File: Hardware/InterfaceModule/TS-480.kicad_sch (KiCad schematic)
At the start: 5 parts, among them J3 TS-480 MIC, J4 TS-480 DATA, J5 TS-480 REMOTE, J6 TS-480 COM, J7 TS-480 EXT.SP

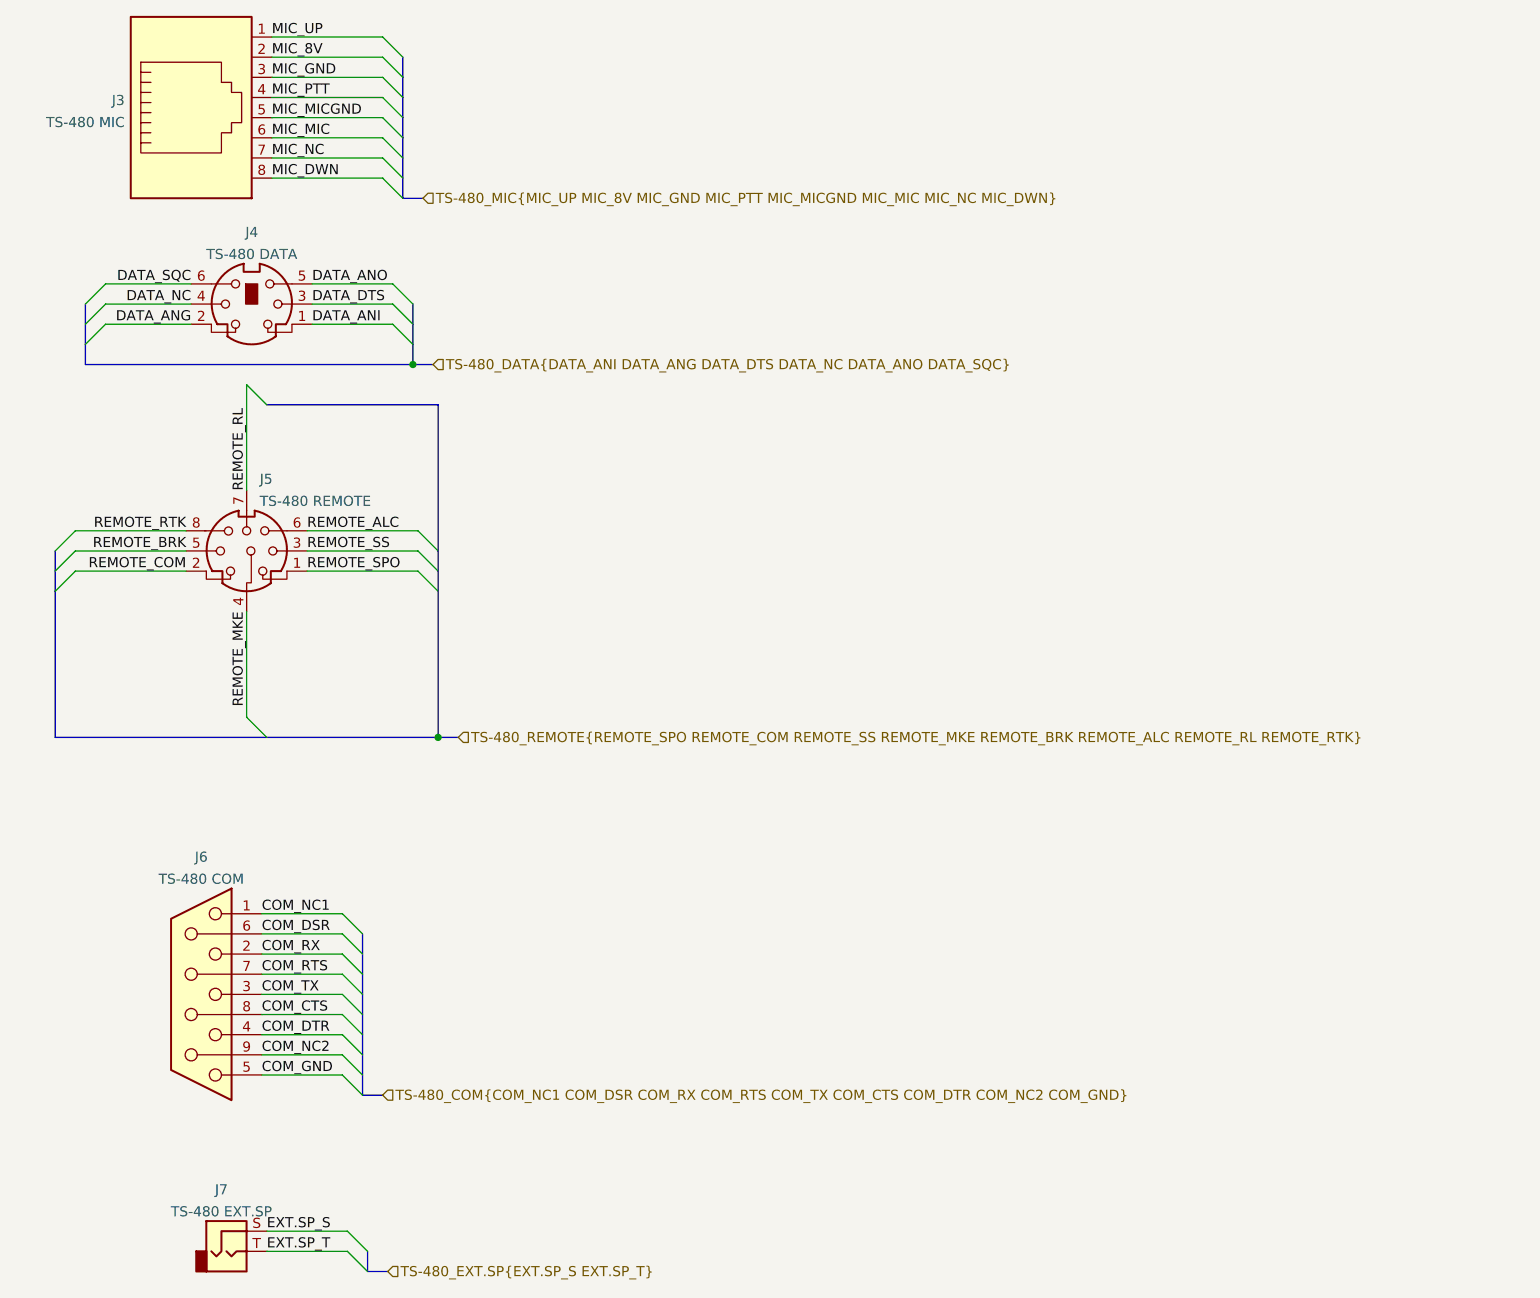
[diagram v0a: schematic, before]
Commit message: Connections for data ports, gps, improved mic connections
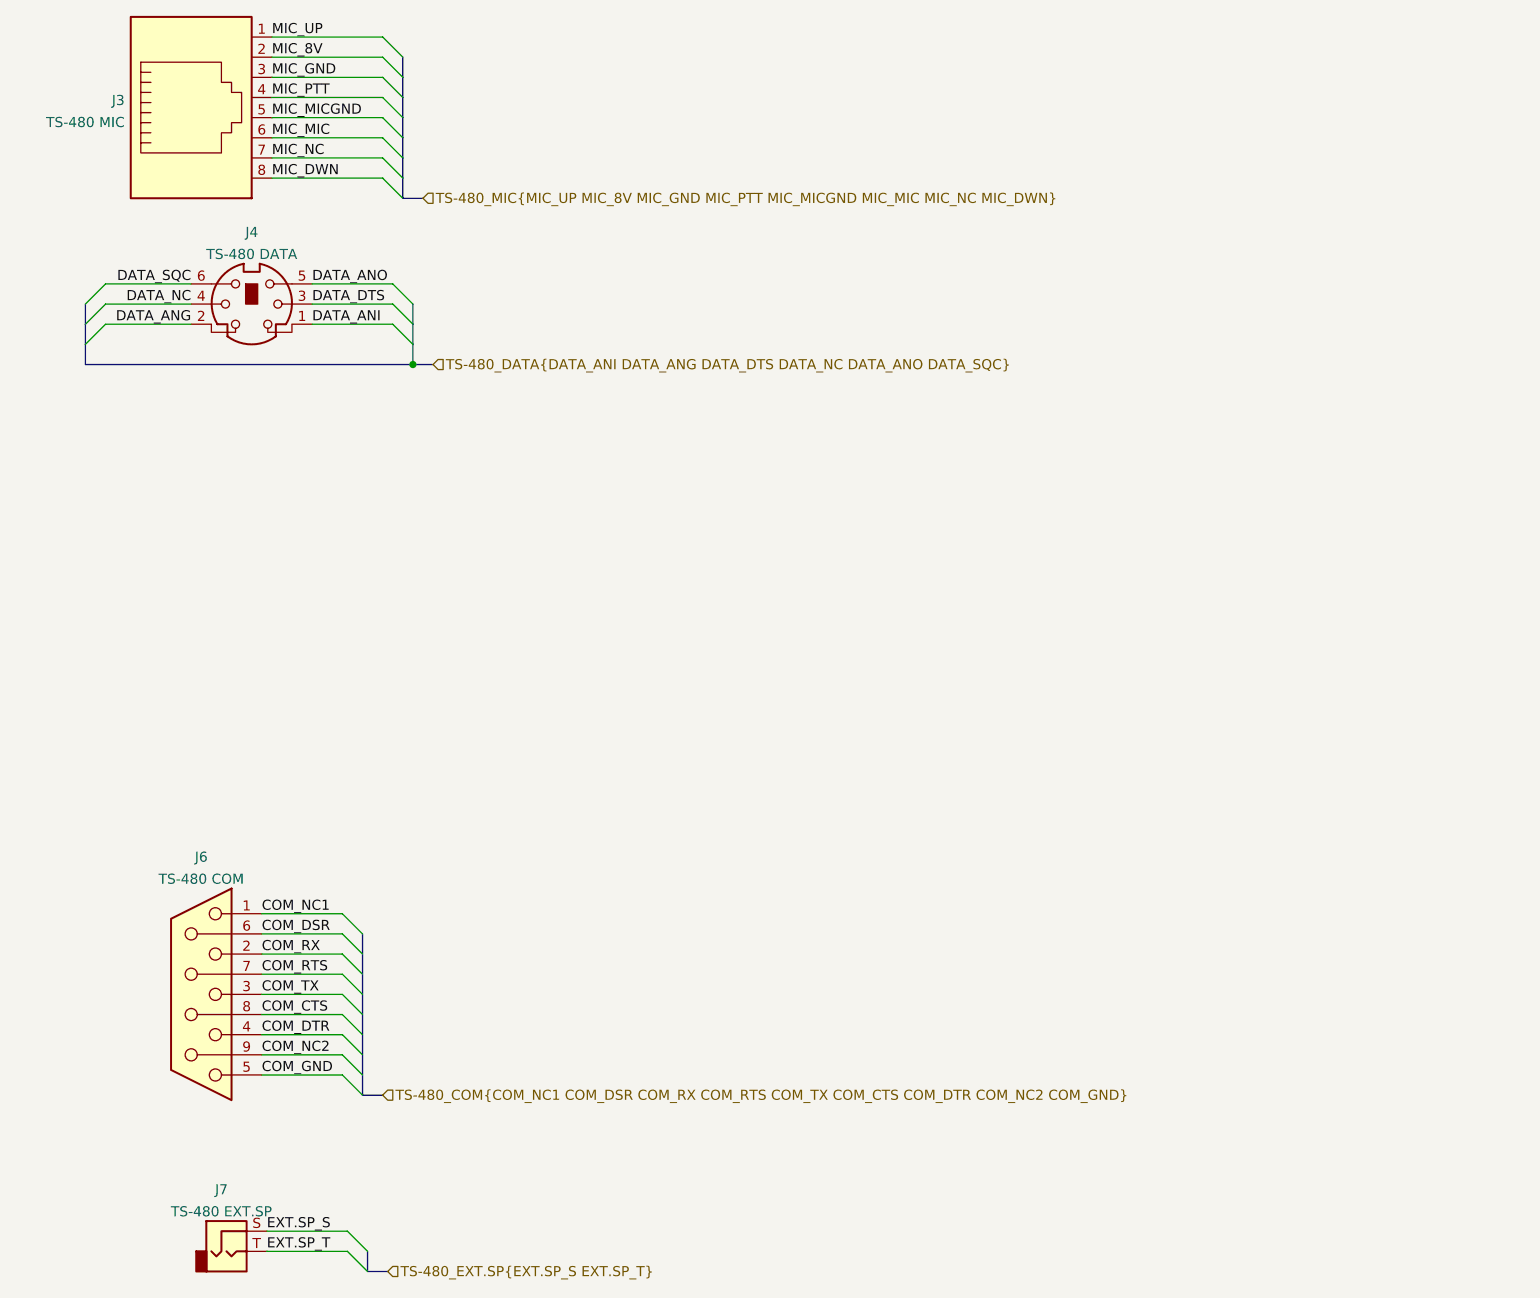
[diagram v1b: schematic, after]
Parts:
- removed J5: TS-480 REMOTE, symbol Connector:Mini-DIN-8
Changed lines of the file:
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@@
 (kicad_sch (version 20211123) (generator eeschema)
   (paper "A4")
-  (junction (at 64.77 107.95) (diameter 0) (color 0 0 0 0)
-  )
   (junction (at 61.595 60.96) (diameter 0) (color 0 0 0 0)
   )
@@
     (stroke (width 0) (type default) (color 0 0 0 0))
   )
-  (bus_entry (at 40.64 63.5) (size 2.54 2.54)
-    (stroke (width 0) (type default) (color 0 0 0 0))
-  )
-  (bus_entry (at 40.64 105.41) (size 2.54 2.54)
-    (stroke (width 0) (type default) (color 0 0 0 0))
-  )
-  (bus_entry (at 19.05 84.455) (size -2.54 2.54)
-    (stroke (width 0) (type default) (color 0 0 0 0))
-  )
-  (bus_entry (at 19.05 81.915) (size -2.54 2.54)
-    (stroke (width 0) (type default) (color 0 0 0 0))
-  )
-  (bus_entry (at 19.05 86.995) (size -2.54 2.54)
-    (stroke (width 0) (type default) (color 0 0 0 0))
-  )
-  (bus_entry (at 62.23 81.915) (size 2.54 2.54)
-    (stroke (width 0) (type default) (color 0 0 0 0))
-  )
-  (bus_entry (at 62.23 84.455) (size 2.54 2.54)
-    (stroke (width 0) (type default) (color 0 0 0 0))
-  )
-  (bus_entry (at 62.23 86.995) (size 2.54 2.54)
-    (stroke (width 0) (type default) (color 0 0 0 0))
-  )
   (bus (pts (xy 20.32 53.34) (xy 20.32 55.88))
     (stroke (width 0) (type default) (color 0 0 0 0))
   )
-  (bus (pts (xy 43.18 66.04) (xy 64.77 66.04))
-    (stroke (width 0) (type default) (color 0 0 0 0))
-  )
   (wire (pts (xy 22.86 50.8) (xy 33.655 50.8))
     (stroke (width 0) (type default) (color 0 0 0 0))
   )
-  (bus (pts (xy 64.77 84.455) (xy 64.77 66.04))
-    (stroke (width 0) (type default) (color 0 0 0 0))
-  )
   (wire (pts (xy 43.815 27.305) (xy 57.785 27.305))
     (stroke (width 0) (type default) (color 0 0 0 0))
@@
     (stroke (width 0) (type default) (color 0 0 0 0))
   )
-  (bus (pts (xy 64.77 107.95) (xy 64.77 89.535))
-    (stroke (width 0) (type default) (color 0 0 0 0))
-  )
   (wire (pts (xy 42.545 140.335) (xy 52.705 140.335))
     (stroke (width 0) (type default) (color 0 0 0 0))
@@
     (stroke (width 0) (type default) (color 0 0 0 0))
   )
-  (wire (pts (xy 40.64 92.075) (xy 40.64 105.41))
-    (stroke (width 0) (type default) (color 0 0 0 0))
-  )
-  (bus (pts (xy 16.51 84.455) (xy 16.51 86.995))
-    (stroke (width 0) (type default) (color 0 0 0 0))
-  )
-  (bus (pts (xy 16.51 107.95) (xy 43.18 107.95))
-    (stroke (width 0) (type default) (color 0 0 0 0))
-  )
   (wire (pts (xy 42.545 137.795) (xy 52.705 137.795))
     (stroke (width 0) (type default) (color 0 0 0 0))
   )
-  (wire (pts (xy 19.05 86.995) (xy 33.02 86.995))
-    (stroke (width 0) (type default) (color 0 0 0 0))
-  )
-  (bus (pts (xy 16.51 86.995) (xy 16.51 89.535))
-    (stroke (width 0) (type default) (color 0 0 0 0))
-  )
   (wire (pts (xy 48.895 55.88) (xy 59.055 55.88))
     (stroke (width 0) (type default) (color 0 0 0 0))
@@
     (stroke (width 0) (type default) (color 0 0 0 0))
   )
-  (wire (pts (xy 19.05 84.455) (xy 33.02 84.455))
-    (stroke (width 0) (type default) (color 0 0 0 0))
-  )
   (bus (pts (xy 60.325 24.765) (xy 60.325 27.305))
     (stroke (width 0) (type default) (color 0 0 0 0))
   )
-  (wire (pts (xy 48.26 81.915) (xy 62.23 81.915))
-    (stroke (width 0) (type default) (color 0 0 0 0))
-  )
   (bus (pts (xy 61.595 55.88) (xy 61.595 58.42))
     (stroke (width 0) (type default) (color 0 0 0 0))
   )
-  (bus (pts (xy 43.18 107.95) (xy 64.77 107.95))
-    (stroke (width 0) (type default) (color 0 0 0 0))
-  )
   (bus (pts (xy 60.325 34.925) (xy 60.325 37.465))
     (stroke (width 0) (type default) (color 0 0 0 0))
@@
     (stroke (width 0) (type default) (color 0 0 0 0))
   )
-  (wire (pts (xy 48.26 86.995) (xy 62.23 86.995))
-    (stroke (width 0) (type default) (color 0 0 0 0))
-  )
   (wire (pts (xy 42.545 147.955) (xy 52.705 147.955))
     (stroke (width 0) (type default) (color 0 0 0 0))
   )
-  (bus (pts (xy 16.51 89.535) (xy 16.51 107.95))
-    (stroke (width 0) (type default) (color 0 0 0 0))
-  )
   (bus (pts (xy 55.245 140.335) (xy 55.245 142.875))
     (stroke (width 0) (type default) (color 0 0 0 0))
@@
     (stroke (width 0) (type default) (color 0 0 0 0))
   )
-  (wire (pts (xy 40.64 63.5) (xy 40.64 76.835))
-    (stroke (width 0) (type default) (color 0 0 0 0))
-  )
   (bus (pts (xy 60.325 22.225) (xy 60.325 24.765))
     (stroke (width 0) (type default) (color 0 0 0 0))
@@
     (stroke (width 0) (type default) (color 0 0 0 0))
   )
-  (wire (pts (xy 19.05 81.915) (xy 33.02 81.915))
-    (stroke (width 0) (type default) (color 0 0 0 0))
-  )
-  (bus (pts (xy 64.77 86.995) (xy 64.77 84.455))
-    (stroke (width 0) (type default) (color 0 0 0 0))
-  )
   (wire (pts (xy 42.545 142.875) (xy 52.705 142.875))
     (stroke (width 0) (type default) (color 0 0 0 0))
   )
-  (bus (pts (xy 64.77 89.535) (xy 64.77 86.995))
-    (stroke (width 0) (type default) (color 0 0 0 0))
-  )
   (bus (pts (xy 55.245 137.795) (xy 55.245 140.335))
     (stroke (width 0) (type default) (color 0 0 0 0))
   )
-  (bus (pts (xy 64.77 107.95) (xy 67.31 107.95))
-    (stroke (width 0) (type default) (color 0 0 0 0))
-  )
   (wire (pts (xy 22.86 55.88) (xy 33.655 55.88))
     (stroke (width 0) (type default) (color 0 0 0 0))
@@
     (stroke (width 0) (type default) (color 0 0 0 0))
   )
-  (wire (pts (xy 48.26 84.455) (xy 62.23 84.455))
-    (stroke (width 0) (type default) (color 0 0 0 0))
-  )
   (bus (pts (xy 20.32 55.88) (xy 20.32 58.42))
     (stroke (width 0) (type default) (color 0 0 0 0))
@@
     (effects (font (size 1.27 1.27)) (justify left bottom))
   )
-  (label "REMOTE_RTK" (at 33.02 81.915 180)
-    (effects (font (size 1.27 1.27)) (justify right bottom))
-  )
-  (label "REMOTE_ALC" (at 48.26 81.915 0)
-    (effects (font (size 1.27 1.27)) (justify left bottom))
-  )
   (label "MIC_NC" (at 43.815 34.925 0)
     (effects (font (size 1.27 1.27)) (justify left bottom))
   )
   (label "COM_DTR" (at 42.545 145.415 0)
-    (effects (font (size 1.27 1.27)) (justify left bottom))
-  )
-  (label "REMOTE_SS" (at 48.26 84.455 0)
     (effects (font (size 1.27 1.27)) (justify left bottom))
   )
@@
     (effects (font (size 1.27 1.27)) (justify right bottom))
   )
-  (label "REMOTE_BRK" (at 33.02 84.455 180)
-    (effects (font (size 1.27 1.27)) (justify right bottom))
-  )
   (label "DATA_ANO" (at 48.895 50.8 0)
     (effects (font (size 1.27 1.27)) (justify left bottom))
@@
     (effects (font (size 1.27 1.27)) (justify left bottom))
   )
-  (label "REMOTE_MKE" (at 40.64 92.075 270)
-    (effects (font (size 1.27 1.27)) (justify right bottom))
-  )
-  (label "REMOTE_RL" (at 40.64 76.835 90)
-    (effects (font (size 1.27 1.27)) (justify left bottom))
-  )
   (label "COM_TX" (at 42.545 140.335 0)
     (effects (font (size 1.27 1.27)) (justify left bottom))
@@
     (effects (font (size 1.27 1.27)) (justify left bottom))
   )
-  (label "REMOTE_SPO" (at 48.26 86.995 0)
-    (effects (font (size 1.27 1.27)) (justify left bottom))
-  )
   (label "COM_NC2" (at 42.545 147.955 0)
     (effects (font (size 1.27 1.27)) (justify left bottom))
@@
   (label "DATA_ANI" (at 48.895 55.88 0)
     (effects (font (size 1.27 1.27)) (justify left bottom))
-  )
-  (label "REMOTE_COM" (at 33.02 86.995 180)
-    (effects (font (size 1.27 1.27)) (justify right bottom))
   )
   (hierarchical_label "TS-480_COM{COM_NC1 COM_DSR COM_RX COM_RTS COM_TX COM_CTS COM_DTR COM_NC2 COM_GND}" (shape input)
@@
     (effects (font (size 1.27 1.27)) (justify left))
   )
-  (hierarchical_label "TS-480_REMOTE{REMOTE_SPO REMOTE_COM REMOTE_SS REMOTE_MKE REMOTE_BRK REMOTE_ALC REMOTE_RL REMOTE_RTK}" (shape input)
-    (at 67.31 107.95 0)
-    (effects (font (size 1.27 1.27)) (justify left))
-  )
-  (symbol (lib_id "Connector:Mini-DIN-8") (at 40.64 84.455 0) (unit 1)
-    (in_bom yes) (on_board yes) (fields_autoplaced)
-    (property "Reference" "J5" (id 0) (at 42.2911 75.4085 0)
-      (effects (font (size 1.27 1.27)) (justify left))
-    )
-    (property "Value" "TS-480 REMOTE" (id 1) (at 42.2911 78.1836 0)
-      (effects (font (size 1.27 1.27)) (justify left))
-    )
-    (property "Footprint" "" (id 2) (at 40.386 84.709 90)
-      (effects (font (size 1.27 1.27)) hide)
-    )
-    (property "Datasheet" "http://service.powerdynamics.com/ec/Catalog17/Section%2011.pdf" (id 3) (at 40.386 84.709 90)
-      (effects (font (size 1.27 1.27)) hide)
-    )
-    (pin "1")
-    (pin "2")
-    (pin "3")
-    (pin "4")
-    (pin "5")
-    (pin "6")
-    (pin "7")
-    (pin "8")
-  )
   (symbol (lib_id "Connector:AudioJack2") (at 38.1 172.72 0) (unit 1)

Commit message: Picked some footprints for most connectors
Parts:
- J7: renamed from J6; footprint (none) -> Connector_Dsub:DSUB-9_Male_Horizontal_P2.77x2.84mm_EdgePinOffset4.94mm_Housed_MountingHolesOffset7.48mm
- J8: renamed from J7; footprint (none) -> Connector_Audio:Jack_3.5mm_Switronic_ST-005-G_horizontal
- renumbered J3 to J5, J4 to J6
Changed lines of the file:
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@@
   (symbol (lib_id "Connector:AudioJack2") (at 38.1 172.72 0) (unit 1)
     (in_bom yes) (on_board yes) (fields_autoplaced)
-    (property "Reference" "J7" (id 0) (at 37.465 164.9435 0))
+    (property "Reference" "J8" (id 0) (at 37.465 164.9435 0))
     (property "Value" "TS-480 EXT.SP" (id 1) (at 37.465 167.7186 0))
-    (property "Footprint" "" (id 2) (at 38.1 172.72 0)
+    (property "Footprint" "Connector_Audio:Jack_3.5mm_Switronic_ST-005-G_horizontal" (id 2) (at 38.1 172.72 0)
       (effects (font (size 1.27 1.27)) hide)
     )
@@
   (symbol (lib_id "Connector:Mini-DIN-6") (at 41.275 53.34 0) (unit 1)
     (in_bom yes) (on_board yes) (fields_autoplaced)
-    (property "Reference" "J4" (id 0) (at 41.2927 44.2935 0))
+    (property "Reference" "J6" (id 0) (at 41.2927 44.2935 0))
     (property "Value" "TS-480 DATA" (id 1) (at 41.2927 47.0686 0))
     (property "Footprint" "" (id 2) (at 41.275 53.34 0)
@@
   (symbol (lib_id "Connector:DB9_Female") (at 34.925 140.335 0) (mirror y) (unit 1)
     (in_bom yes) (on_board yes) (fields_autoplaced)
-    (property "Reference" "J6" (id 0) (at 34.925 123.0335 0))
+    (property "Reference" "J7" (id 0) (at 34.925 123.0335 0))
     (property "Value" "TS-480 COM" (id 1) (at 34.925 125.8086 0))
-    (property "Footprint" "" (id 2) (at 34.925 140.335 0)
+    (property "Footprint" "Connector_Dsub:DSUB-9_Male_Horizontal_P2.77x2.84mm_EdgePinOffset4.94mm_Housed_MountingHolesOffset7.48mm" (id 2) (at 34.925 140.335 0)
       (effects (font (size 1.27 1.27)) hide)
     )
@@
   (symbol (lib_id "Connector:RJ45") (at 33.655 27.305 0) (mirror x) (unit 1)
     (in_bom yes) (on_board yes) (fields_autoplaced)
-    (property "Reference" "J3" (id 0) (at 25.2731 27.6665 0)
+    (property "Reference" "J5" (id 0) (at 25.2731 27.6665 0)
       (effects (font (size 1.27 1.27)) (justify right))
     )

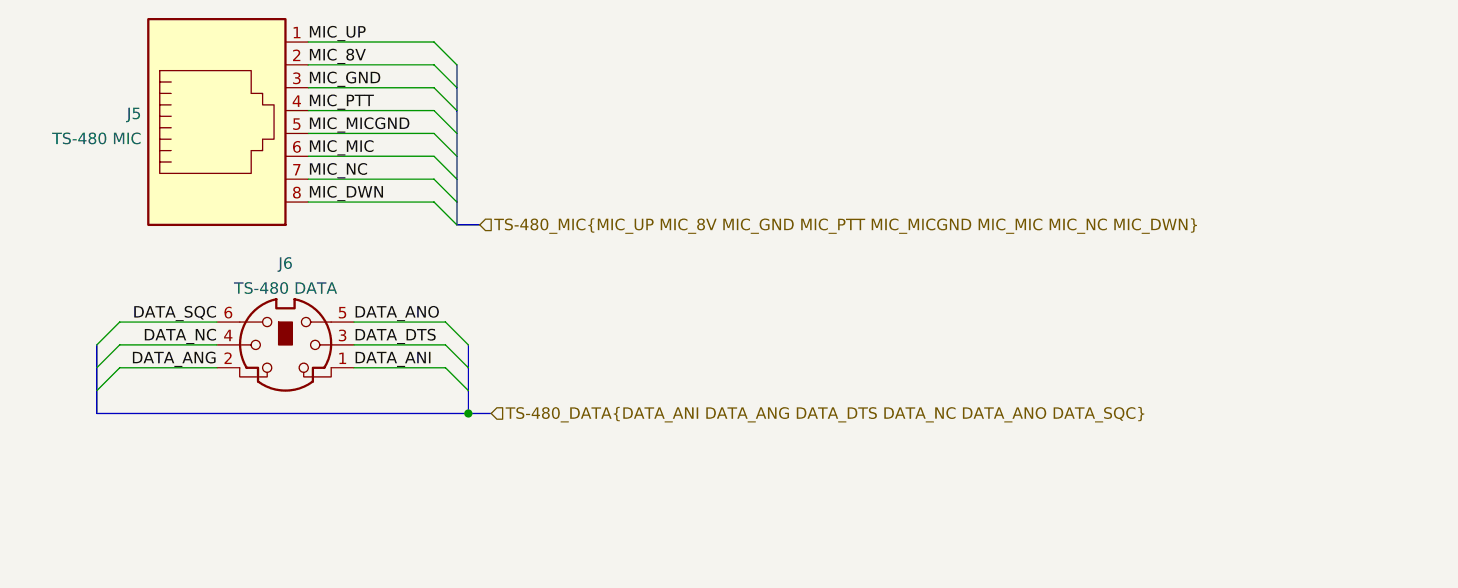
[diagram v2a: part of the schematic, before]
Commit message: Redesigned layout and labels
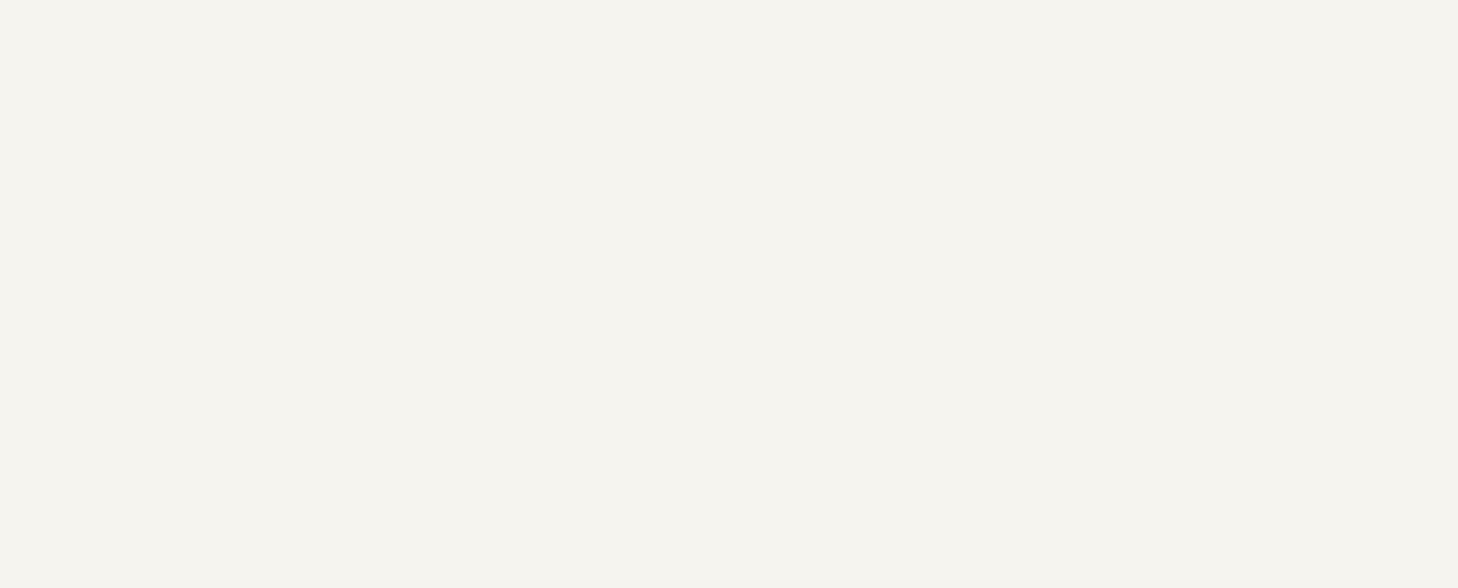
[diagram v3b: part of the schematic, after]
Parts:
- removed J5: TS-480 MIC, Connector_RJ:RJ45_Amphenol_54602-x08_Horizontal, symbol Connector:RJ45
- removed J6: TS-480 DATA, symbol Connector:Mini-DIN-6
